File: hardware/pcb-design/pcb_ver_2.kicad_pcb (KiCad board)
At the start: 2 copper layers, 71.5 x 54 mm, 34 parts, among them J1 GTFP08441BEU, J2 Conn_01x04_Pin, J3 USB4085-GF-A_REVA4, J4 Conn_01x07_Socket, J5 Screw_Terminal_01x02, J6 UART, Q1 NMOS, U1 ESP32-S3-WROOM-2, U2 LM1117MP-3.3

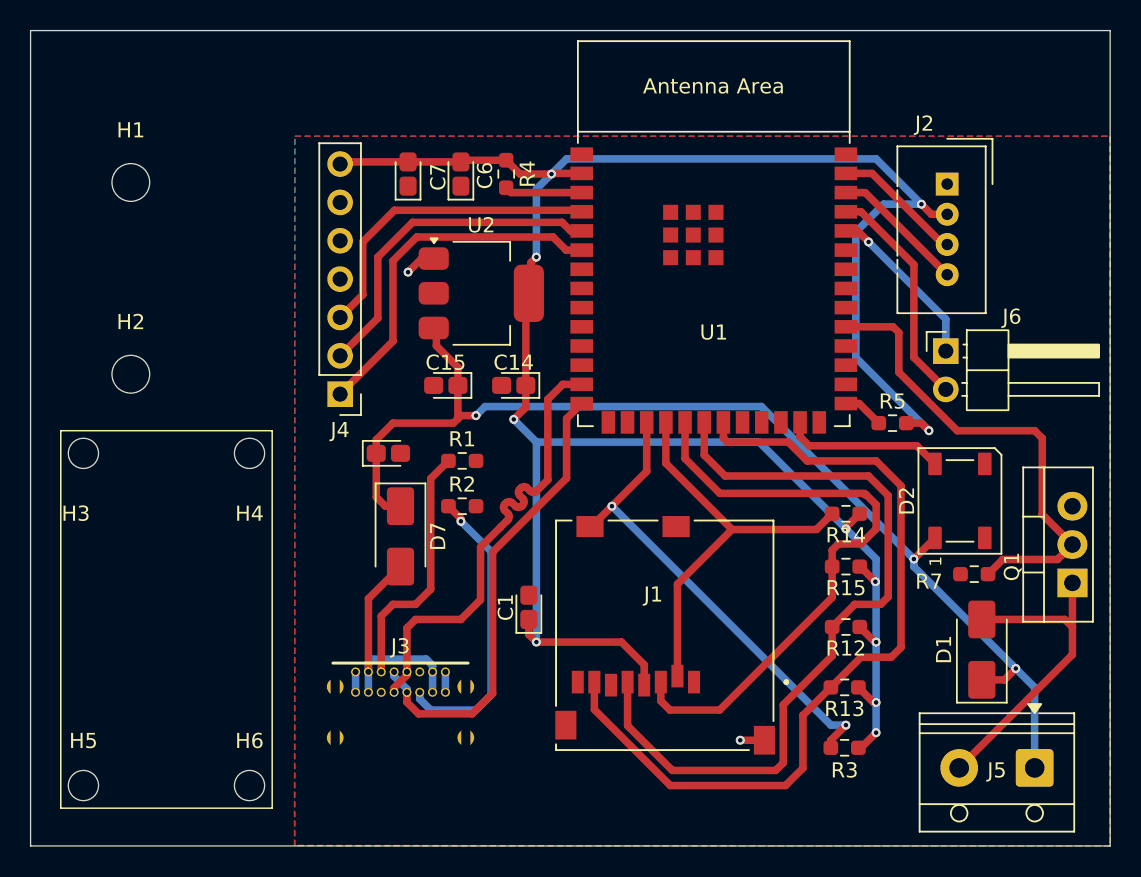
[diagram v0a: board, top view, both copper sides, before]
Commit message: hardware: change to USB board
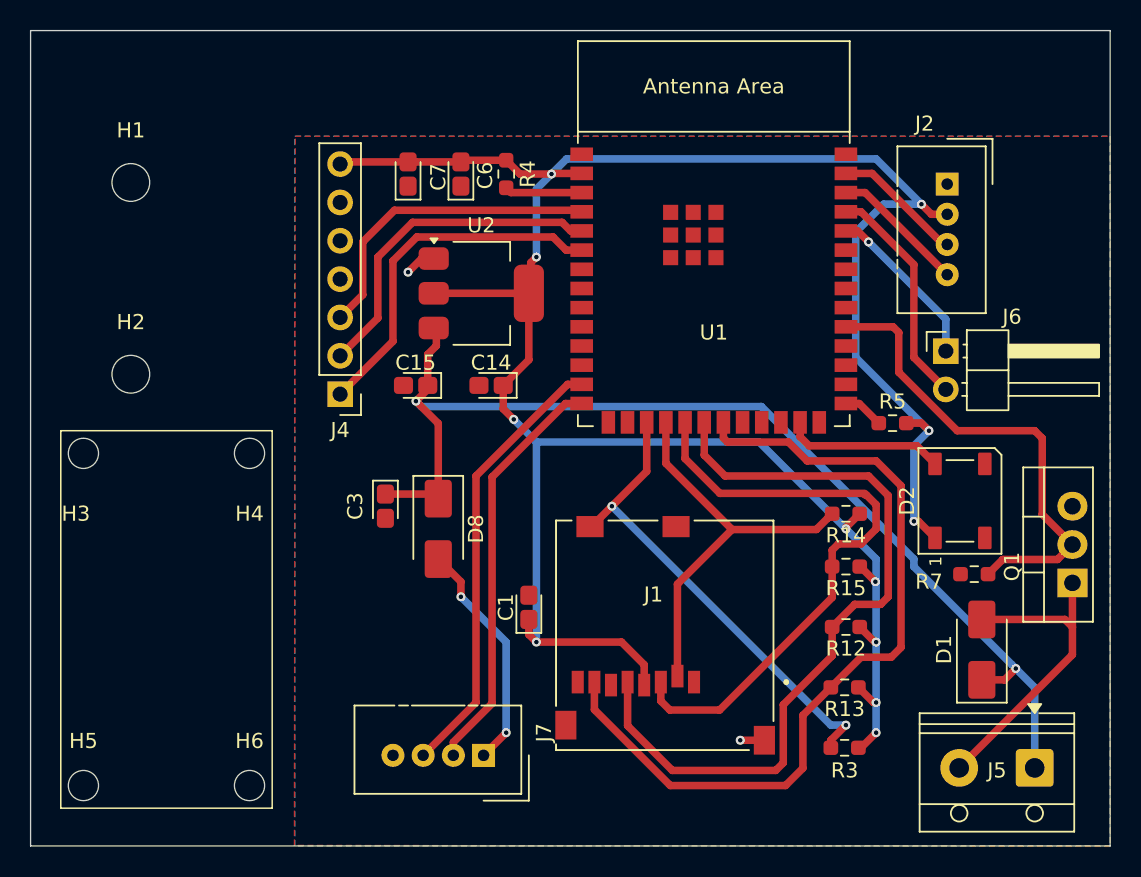
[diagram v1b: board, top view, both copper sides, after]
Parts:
- removed C2: 10uF, Capacitor_Tantalum_SMD:CP_EIA-1608-10_AVX-L_HandSolder
- removed D7: SS34, Diode_SMD:D_SMA
- removed J3: USB4085-GF-A_REVA4, USB4085-GF-A:GCT_USB4085-GF-A_REVA
- removed R1, R2: 5k1, Resistor_SMD:R_0603_1608Metric_Pad0.98x0.95mm_HandSolder
- added C3: 10uF, Capacitor_Tantalum_SMD:CP_EIA-1608-10_AVX-L_HandSolder, F.Cu at (91.0, 62.0)
- added D8: SS34, Diode_SMD:D_SMA, F.Cu at (94.5, 63.5)
- added J7: Conn_01x04_Socket, Connector:NS-Tech_Grove_1x04_P2mm_Vertical, F.Cu at (97.5, 78.5)
- Q1: value NMOS -> HUF76423P
- moved C15 2.00 mm to (93.0, 54.0)
- moved C14 1.50 mm to (98.0, 54.0)
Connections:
- D2 pad 1: +5V -> +3.3V
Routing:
- net Net-(J3-CC2): track 19.6 -> 0.00 mm, vias 1 -> 0
- net Net-(J3-CC1): track 16.7 -> 0.00 mm
- net VBUS: track 16.1 -> 0.00 mm
- net +3.3V: track 154.8 -> 170.4 mm, vias 11 -> 12
- net Net-(D8-A): track 0.00 -> 15.5 mm, vias 0 -> 2
- net /D+: track 30.6 -> 27.4 mm
- net GND: track 6.37 -> 3.67 mm
- net +5V: track 74.5 -> 73.0 mm, vias 3 -> 2
- net /D-: track 30.5 -> 29.5 mm

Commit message: hardware: remove vias and change sizes
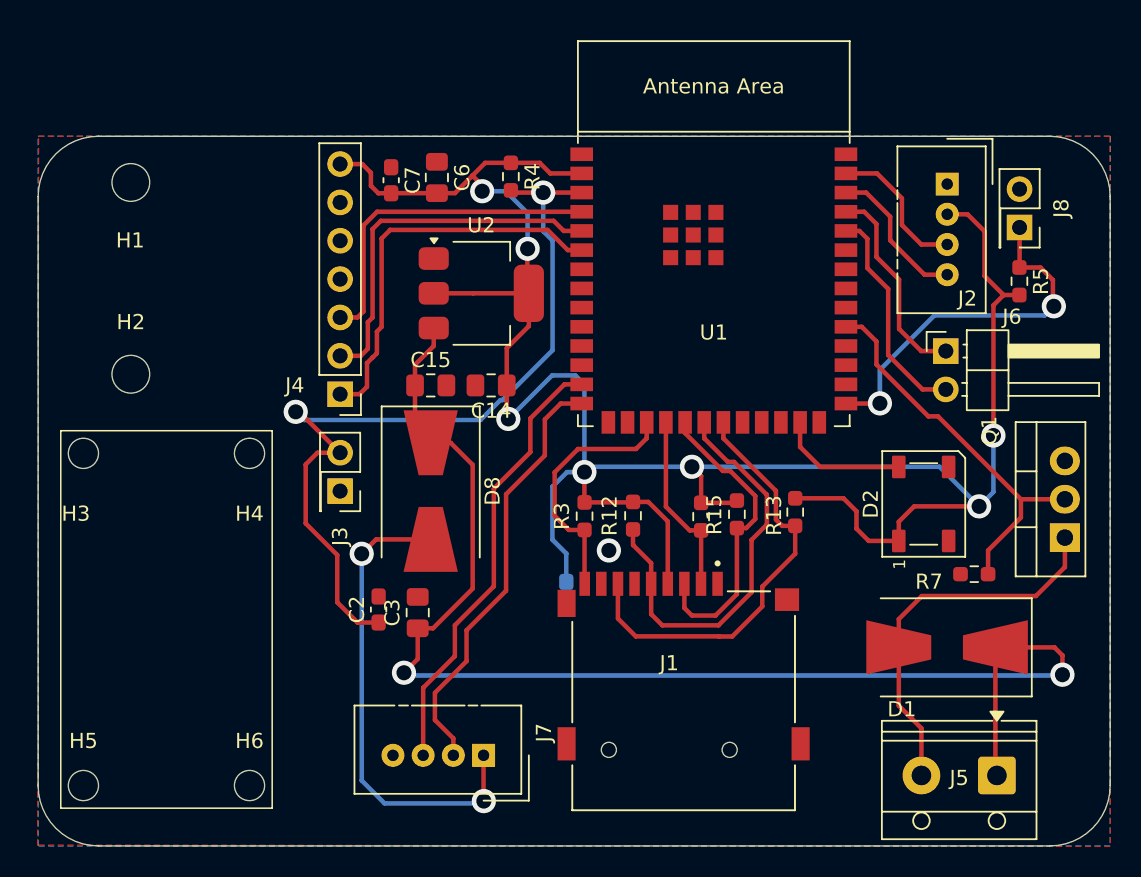
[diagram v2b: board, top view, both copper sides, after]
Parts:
- added C2: 1u, Capacitor_SMD:C_0603_1608Metric_Pad1.08x0.95mm_HandSolder, F.Cu at (90.5, 68.8)
- added J3: Conn_01x02_Pin, Connector_PinSocket_2.54mm:PinSocket_2x01_P2.54mm_Vertical, F.Cu at (88.0, 61.0)
- added J8: Conn_01x02_Pin, Connector_PinSocket_2.54mm:PinSocket_2x01_P2.54mm_Vertical, F.Cu at (133.0, 43.5)
- C1: footprint Capacitor_Tantalum_SMD:CP_EIA-1608-10_AVX-L_HandSolder -> Capacitor_SMD:C_0603_1608Metric_Pad1.08x0.95mm_HandSolder; moved to B.Cu
- C14, C15, C3, C6: footprint Capacitor_Tantalum_SMD:CP_EIA-1608-10_AVX-L_HandSolder -> Capacitor_SMD:C_0805_2012Metric_Pad1.18x1.45mm_HandSolder
- C7: footprint Capacitor_Tantalum_SMD:CP_EIA-1608-10_AVX-L_HandSolder -> Capacitor_SMD:C_0603_1608Metric_Pad1.08x0.95mm_HandSolder
- D1, D8: footprint Diode_SMD:D_SMA -> Diode_SMD:D_SMB-SMC_Universal_Handsoldering
- J1: value GTFP08441BEU -> MSD-4-A; footprint GTFP08441BEU:AMPHENOL_GTFP08441BEU -> MSD-4-A:CUI_MSD-4-A
- R3: value R -> 10k
- moved R3 23.1 mm to (104.2, 62.7), turned to -90 degrees
- moved R12 15.9 mm to (107.4, 62.6), turned to -90 degrees
- moved R5 12.6 mm to (133.0, 47.1), turned to -90 degrees
- moved R13 12.1 mm to (118.1, 62.4), turned to -90 degrees
- moved R14 9.59 mm to (111.9, 62.7), turned to -90 degrees
- moved R15 8.01 mm to (114.3, 62.5), turned to -90 degrees
- moved C3 7.37 mm to (93.1, 69.0), turned to 90 degrees
- moved Q1 3.04 mm to (136.0, 64.1)
- moved C1 2.61 mm to (103.0, 67.9), turned to -90 degrees
- moved D8 2.55 mm to (94.0, 61.0)
- moved J5 2.55 mm to (131.5, 79.8)
- moved D2 2.41 mm to (126.7, 61.9)
- moved D1 2.30 mm to (128.2, 71.3), turned to 180 degrees
- moved J1 2.04 mm to (110.8, 74.9)
- moved C6 1.61 mm to (94.4, 40.2), turned to -90 degrees
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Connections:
- net Net-(U1-EN) renamed /EN
- net Net-(U1-GPIO0/BOOT) renamed /BOOT
- R3 pad 1: /SD_CD -> +3.3V
- R3 pad 2: +3.3V -> /SD_CD
- U1 pad 36: Net-(J6-Pin_1) -> Net-(J6-Pin_2)
- U1 pad 37: Net-(J6-Pin_2) -> Net-(J6-Pin_1)
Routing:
- net /EN: track 5.13 -> 54.5 mm, vias 0 -> 2
- net /SD_MISO: track 54.9 -> 28.7 mm
- net /SD_SCLK: track 51.7 -> 27.6 mm
- net /BOOT: track 2.71 -> 24.7 mm, vias 0 -> 2
- net +3.3V: track 170.4 -> 149.5 mm, vias 12 -> 7
- net /SD_MOSI: track 40.4 -> 20.3 mm
- net Net-(D8-A): track 15.5 -> 31.8 mm
- net /SD_CS: track 27.6 -> 12.1 mm
- net /SD_CD: track 31.9 -> 16.9 mm, vias 2 -> 0
- net +5V: track 73.0 -> 86.3 mm
- net /MOT_SWITCH: track 31.9 -> 26.0 mm
- net Net-(D1-A): track 21.6 -> 25.4 mm
- net GND: track 3.67 -> 0.00 mm, vias 2 -> 1
- net Net-(J6-Pin_1): track 11.1 -> 13.6 mm, vias 1 -> 0
- net /AMP_LRCLK: track 23.8 -> 26.3 mm
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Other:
- board size 71.5 x 54 mm -> 71 x 47 mm
